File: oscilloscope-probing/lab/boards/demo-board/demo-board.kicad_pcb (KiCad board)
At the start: 8 copper layers, 126 x 117 mm, 298 parts, among them J1 CONN_01X03, J10 SMA-J-P-H-ST-EM1, J11 TESTCLIP, J12 TESTCLIP, J13 TESTCLIP, J14 USB_C_Receptacle_USB2.0, J15 TESTCLIP, J16 SMA-J-P-H-ST-EM1, J17 SMA-J-P-H-ST-EM1, J18 SMA-J-P-H-ST-EM1, J19 SMA-J-P-H-ST-EM1, J2 CORTEX_DEBUG_ETM, J20 SMA-J-P-H-ST-EM1, J21 SMA-J-P-H-ST-EM1, J3 XILINX_JTAG, J4 CORTEX_DEBUG_ETM, J5 DISPLAY, J6 CONN_01X06, J7 SMA-J-P-H-ST-EM1, J8 SMA-J-P-H-ST-EM1, J9 SMA-J-P-H-ST-EM1, M1 LOGO, M2 LOGO, M3 LOGO, M4 LOGO, Q1 SSM6N58NU, SW1 SWITCH, SW2 SWITCH, SW3 SWITCH, SW4 SWITCH, SW5 SWITCH, SW6 SWITCH, SW7 SWITCH, U1 FT234XD, U10 19-C47/RSGHBHC-5V01/2T, U11 19-C47/RSGHBHC-5V01/2T, U12 19-C47/RSGHBHC-5V01/2T, U13 19-C47/RSGHBHC-5V01/2T, U2 STM32L431-QFN48, U26 74LVC1T45, U3 LTC3374A, U39 NCP45525IMNTWG-H, U4 XC7A35T-2FGG484I, U5 STM32H750XBH6, U6 ECS-1612MV-250-CN, U7 ECS-1612MV-250-CN, U8 S25FL064LABMFI013, U9 SIT9121AI-2BF-XXS156.250000G

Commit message: Continued demo board layout
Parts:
- added C124: 0.1 uF, azonenberg_pcb:EIA_0402_CAP_NOSILK, F.Cu at (33.0, 92.5)
- added C125: 0.1 uF, azonenberg_pcb:EIA_0402_CAP_NOSILK, F.Cu at (33.0, 76.5)
- added J22: SMA-J-P-H-ST-EM1, azonenberg_pcb:CONN_SMA_EDGE_SAMTEC_SMA_J_P_H_ST_EM1, F.Cu at (60.5, 29.5)
- added J23: SMA-J-P-H-ST-EM1, azonenberg_pcb:CONN_SMA_EDGE_SAMTEC_SMA_J_P_H_ST_EM1, F.Cu at (60.5, 35.5)
- C16, C17, C53, R37, R5: moved to B.Cu
- moved TP2 144.0 mm to (57.2, 81.5), turned to 90 degrees
- moved R37 134.5 mm to (59.0, 59.5), turned to -90 degrees
- moved J6 123.3 mm to (76.5, 37.0), turned to 180 degrees
- moved C16 114.0 mm to (59.2, 65.5)
- moved C17 114.0 mm to (59.2, 67.5)
- moved C53 113.6 mm to (61.5, 60.5)
- moved R35 99.2 mm to (76.2, 70.8), turned to 180 degrees
- moved TP8 77.4 mm to (97.5, 87.5), turned to 180 degrees
- moved D4 13.2 mm to (110.2, 63.8)
- moved D5 13.2 mm to (110.2, 64.8)
- moved D6 13.2 mm to (110.2, 65.8)
- moved D7 13.2 mm to (110.2, 66.8)
- moved R39 13.2 mm to (108.2, 63.8)
- moved R41 13.2 mm to (108.2, 64.8)
- moved R42 13.2 mm to (108.2, 65.8)
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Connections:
- J20 pad 1: /Test signals/2XTHRU -> /Test signals/GTP_TX1_AC_P
- J21 pad 1: /Test signals/2XTHRU -> /Test signals/GTP_TX1_AC_N
- U2 pad 29: unconnected-(U2A-PA8-Pad29) -> /MCU/MCU_RST_N
- U2 pad 32: unconnected-(U2A-PA11-Pad32) -> /FPGA support/FPGA_RST_N
- U2 pad 41: /MCU/MCU_RST_N -> /FPGA support/FPGA_INIT
- U2 pad 42: /FPGA support/FPGA_RST_N -> /Power Supply/SUPER_I2C_SCL
- U2 pad 43: /FPGA support/FPGA_INIT -> /Power Supply/SUPER_I2C_SDA
- U4 pad AA18: /MCU/FMC_NE3 -> /MCU/FMC_A17
- U4 pad AA20: /MCU/FMC_NOE -> /MCU/FMC_A16
- U4 pad AA21: /MCU/FMC_NWE -> /MCU/FMC_AD1
- U4 pad AB18: /MCU/FMC_AD0 -> /MCU/FMC_A18
- U4 pad AB20: /MCU/FMC_NE4 -> /MCU/FMC_AD14
- U4 pad AB21: /MCU/FMC_A16 -> /MCU/FMC_AD13
- U4 pad AB22: /MCU/FMC_A17 -> /MCU/FMC_AD15
- U4 pad C5: unconnected-(U4I-GTP_TX_1_N-PadC5) -> /Test signals/GTP_TX1_N
- U4 pad D5: unconnected-(U4I-GTP_TX_1_P-PadD5) -> /Test signals/GTP_TX1_P
- U4 pad N13: /MCU/FMC_AD11 -> /MCU/FMC_NBL0
- U4 pad N14: /MCU/FMC_AD12 -> /MCU/FMC_NBL1
- U4 pad N15: /MCU/FMC_AD15 -> /MCU/FMC_NE3
- U4 pad P15: /MCU/FMC_AD9 -> /MCU/FMC_A22
- U4 pad P16: /MCU/FMC_AD13 -> /MCU/FMC_NOE
- U4 pad P17: /MCU/FMC_AD8 -> /MCU/FMC_AD6
- U4 pad R14: /MCU/FMC_AD4 -> /MCU/FMC_NL_NADV
- U4 pad R16: /MCU/FMC_AD10 -> /MCU/FMC_NWAIT
- U4 pad R17: /MCU/FMC_AD14 -> /MCU/FMC_NE4
- U4 pad R18: /MCU/FMC_AD5 -> /MCU/FMC_A20
- U4 pad T18: /MCU/FMC_AD6 -> /MCU/FMC_AD8
- U4 pad U17: /MCU/FMC_AD1 -> /MCU/FMC_NWE
- U4 pad U20: /MCU/FMC_A18 -> /MCU/FMC_NE2
- U4 pad U21: /MCU/FMC_A22 -> /MCU/FMC_AD9
- U4 pad V22: /MCU/FMC_A20 -> /MCU/FMC_AD5
- U4 pad W17: /MCU/FMC_NE2 -> /MCU/FMC_AD0
- U4 pad W21: /MCU/FMC_NL_NADV -> /MCU/FMC_AD4
- U4 pad W22: /MCU/FMC_NWAIT -> /MCU/FMC_AD10
- U4 pad Y21: /MCU/FMC_NBL0 -> /MCU/FMC_AD11
- U4 pad Y22: /MCU/FMC_NBL1 -> /MCU/FMC_AD12
- U5 pad A2: unconnected-(U5I-PI6-PadA2) -> /MCU/MCU_LED0
- U5 pad A3: unconnected-(U5I-PI5-PadA3) -> /MCU/MCU_LED1
- U5 pad A4: unconnected-(U5I-PI4-PadA4) -> /MCU/MCU_LED2
- U5 pad A5: unconnected-(U5B-PB5-PadA5) -> /MCU/MCU_LED3
- U5 pad N6: /MCU/MCU_LED0 -> unconnected-(U5J-PJ0-PadN6)
- U5 pad P6: /MCU/MCU_LED1 -> unconnected-(U5J-PJ1-PadP6)
- U5 pad T6: /MCU/MCU_LED2 -> unconnected-(U5J-PJ2-PadT6)
- U5 pad U6: /MCU/MCU_LED3 -> unconnected-(U5J-PJ3-PadU6)
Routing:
- net /GND: track 827.9 -> 874.3 mm, vias 373 -> 378
- net /MCU/DPAD_N: track 20.5 -> 59.5 mm
- net /MCU/DPAD_W: track 33.2 -> 71.4 mm
- net /MCU/DPAD_SEL: track 27.0 -> 64.9 mm
- net /MCU/DPAD_S: track 35.7 -> 72.6 mm
- net /MCU/DPAD_E: track 24.8 -> 60.7 mm
- net /Power Supply/1V0_FB: track 2.79 -> 36.8 mm, vias 2 -> 3
- net /USB power inlet and UART/UART_TX: track 12.9 -> 45.6 mm
- net /MCU/FMC_AD7: track 0.00 -> 32.0 mm
- net /USB power inlet and UART/UART_RX: track 17.5 -> 47.7 mm
- net /MCU/FMC_AD6: track 0.00 -> 30.1 mm
- net /MCU/FMC_AD0: track 5.03 -> 34.0 mm
- net /USB power inlet and UART/UART_RTS_N: track 21.9 -> 49.6 mm
- net /USB power inlet and UART/UART_CTS_N: track 22.8 -> 49.3 mm
- net /MCU/FMC_A18: track 2.00 -> 28.2 mm
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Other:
- board text added: "1V0"
- board text added: "MCU LED"
- board text added: "MCU UART"
- board text added: "SCL"
- board text added: "SDA"
- board text added: "SUPER STATUS"

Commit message: Continued routing demo board
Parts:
- C90, C92, C95, R38, U9: moved to B.Cu
- moved U9 148.7 mm to (42.9, 62.0)
- moved C90 148.2 mm to (40.0, 62.0), turned to 90 degrees
- moved C95 142.9 mm to (46.2, 61.0)
- moved C92 142.3 mm to (46.2, 62.5)
- moved R22 130.1 mm to (69.2, 88.6)
- moved R23 129.8 mm to (69.2, 89.6), turned to 180 degrees
- moved R24 127.5 mm to (69.2, 86.2)
- moved R25 127.3 mm to (69.2, 87.2), turned to 180 degrees
- moved J3 114.2 mm to (54.5, 43.5), turned to 180 degrees
- moved TP9 79.1 mm to (110.8, 78.2), turned to -90 degrees
- moved R38 71.1 mm to (104.4, 69.0), turned to 90 degrees
- moved U26 50.4 mm to (222.8, 70.0)
- moved C65 33.2 mm to (90.2, 66.2), turned to 180 degrees
- moved C64 27.9 mm to (101.8, 79.2), turned to -90 degrees
- moved J4 27.0 mm to (136.2, 68.5), turned to 90 degrees
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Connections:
- U4 pad F21: unconnected-(U4F-IO_25_16-PadF21) -> /Test signals/LED_CTRL
- U5 pad D10: /MCU/DPAD_SEL -> unconnected-(U5J-PJ14-PadD10)
- U5 pad D11: /MCU/DPAD_S -> unconnected-(U5J-PJ12-PadD11)
- U5 pad E10: /MCU/DPAD_N -> unconnected-(U5J-PJ13-PadE10)
- U5 pad L14: /MCU/DPAD_W -> /MCU/DPAD_S
- U5 pad M14: unconnected-(U5J-PJ9-PadM14) -> /MCU/DPAD_SEL
- U5 pad N14: unconnected-(U5J-PJ7-PadN14) -> /MCU/DPAD_W
- U5 pad N15: unconnected-(U5J-PJ6-PadN15) -> /MCU/DPAD_N
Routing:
- net /MCU/TRACED3: track 0.00 -> 42.2 mm, vias 0 -> 2
- net /GND: track 874.3 -> 915.8 mm, vias 378 -> 394
- net /MCU/TRACED2: track 0.00 -> 41.2 mm, vias 0 -> 2
- net /MCU/TRACED0: track 0.00 -> 35.5 mm, vias 1 -> 2
- net /MCU/TRACED1: track 0.00 -> 35.3 mm, vias 1 -> 2
- net /MCU/JTAG_TDO: track 0.00 -> 34.2 mm, vias 0 -> 2
- net /Power Supply/SUPER_I2C_SDA: track 5.68 -> 37.2 mm, vias 1 -> 2
- net /Power Supply/SUPER_I2C_SCL: track 7.99 -> 38.4 mm, vias 1 -> 2
- net /MCU/DPAD_E: track 60.7 -> 86.7 mm
- net /MCU/DPAD_S: track 72.6 -> 97.4 mm
- net /MCU/DPAD_SEL: track 64.9 -> 88.5 mm
- net /MCU/DPAD_W: track 71.4 -> 94.2 mm
- net /MCU/TRACECLK: track 8.48 -> 31.0 mm, vias 1 -> 2
- net /MCU/DPAD_N: track 59.5 -> 80.4 mm
- net /3V3: track 561.4 -> 578.8 mm, vias 90 -> 93
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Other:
- board text added: "MCU DEBUG"
- board text added: "VCORE"

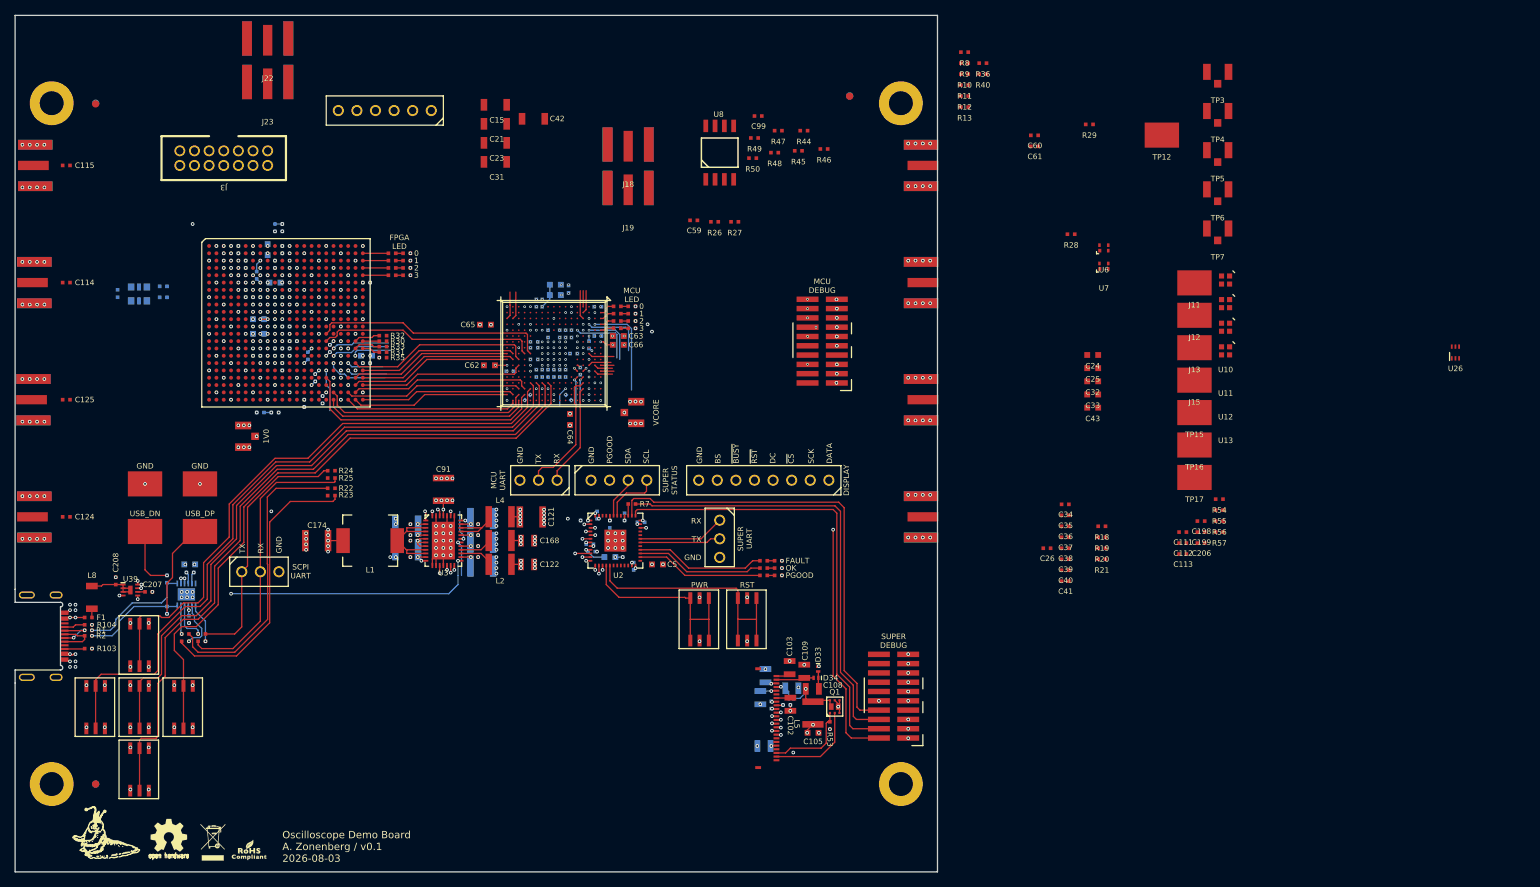
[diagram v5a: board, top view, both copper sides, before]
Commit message: Continued demo board layout
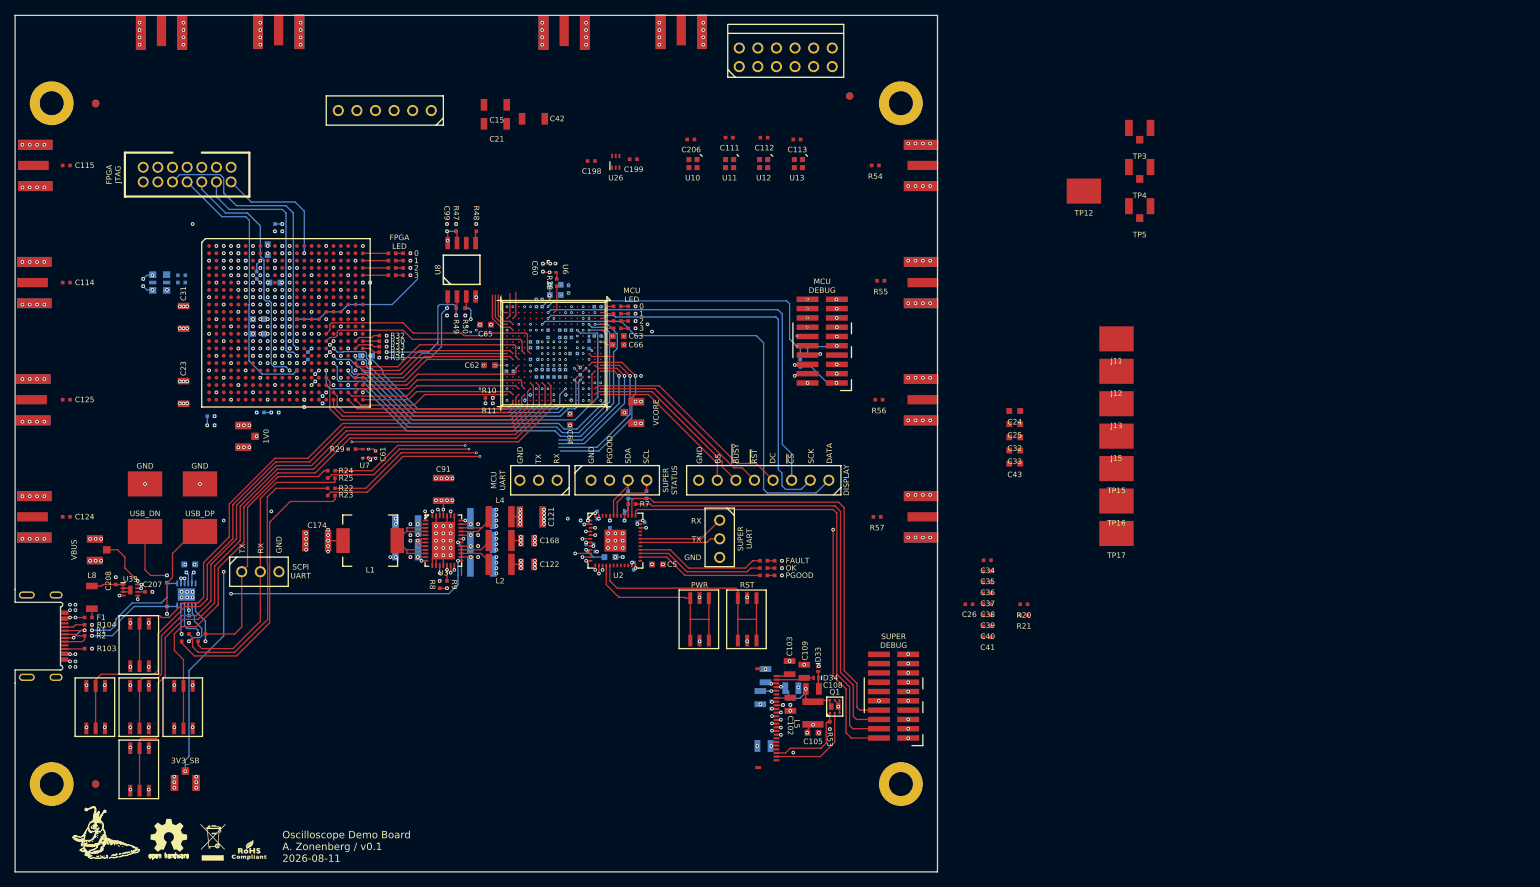
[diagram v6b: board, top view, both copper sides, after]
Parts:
- added J24: PMOD_HOST, azonenberg_pcb:CONN_HEADER_2.54MM_2x6_RA_PMOD_HOST, F.Cu at (131.3, 29.7)
- C59, R12, R13, R18, R19, R26, R27, R36, R40, R44, R45, R46: moved to B.Cu
- J18, J19, J22, J23: footprint azonenberg_pcb:CONN_SMA_EDGE_SAMTEC_SMA_J_P_H_ST_EM1 -> azonenberg_pcb:CONN_SMA_EDGE_SAMTEC_SMA_J_P_H_ST_EM1_NOPASTE
- moved TP6 161.0 mm to (37.0, 97.0), turned to 90 degrees
- moved TP7 160.0 mm to (49.2, 128.8), turned to 180 degrees
- moved U26 117.6 mm to (108.0, 44.0)
- moved R19 114.4 mm to (64.0, 65.5), turned to 180 degrees
- moved R18 112.1 mm to (64.5, 72.0), turned to 90 degrees
- moved R12 111.8 mm to (52.8, 78.8), turned to 180 degrees
- moved R13 111.7 mm to (52.8, 80.0)
- moved R29 110.1 mm to (72.0, 83.2)
- moved U7 104.0 mm to (73.9, 83.8), turned to 90 degrees
- moved R8 102.1 mm to (84.0, 101.8), turned to 90 degrees
- moved R9 100.4 mm to (85.0, 101.8), turned to -90 degrees
- moved C61 99.4 mm to (75.2, 84.0), turned to 90 degrees
- moved C198 96.7 mm to (104.7, 43.9)
- moved C199 92.8 mm to (110.5, 43.6)
- moved C206 88.9 mm to (118.3, 41.0)
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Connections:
- C92 pad 2: /Test signals/GTP_REF_P -> /Test signals/GTP_REF_N
- C95 pad 2: /Test signals/GTP_REF_N -> /Test signals/GTP_REF_P
- J6 pad 2: /MCU/FPGA_UART_CTS_N -> /Test signals/FPGA_UART_CTS_N
- J6 pad 4: /MCU/FPGA_UART_TX -> /Test signals/FPGA_UART_TX
- J6 pad 5: /MCU/FPGA_UART_RX -> /Test signals/FPGA_UART_RX
- J6 pad 6: /MCU/FPGA_UART_RTS_N -> /Test signals/FPGA_UART_RTS_N
- U4 pad A18: unconnected-(U4F-IO_L17P_T2_16-PadA18) -> /Test signals/FPGA_UART_CTS_N
- U4 pad A19: unconnected-(U4F-IO_L17N_T2_16-PadA19) -> /Test signals/FPGA_UART_TX
- U4 pad A20: unconnected-(U4F-IO_L16N_T2_16-PadA20) -> /Test signals/FPGA_UART_RTS_N
- U4 pad A21: unconnected-(U4F-IO_L21N_T3_DQS_16-PadA21) -> /Test signals/FPGA_UART_RX
- U4 pad AA19: /MCU/FPGA_UART_RTS_N -> unconnected-(U4D-IO_L15P_T2_DQS_RDWR_B_14-PadAA19)
- U4 pad N13: /MCU/FMC_NBL0 -> /MCU/FMC_A21
- U4 pad N14: /MCU/FMC_NBL1 -> /MCU/FMC_A20
- U4 pad N15: /MCU/FMC_NE3 -> /MCU/FMC_A19
- U4 pad P15: /MCU/FMC_A22 -> /MCU/FMC_AD8
- U4 pad P19: /MCU/FPGA_UART_TX -> unconnected-(U4D-IO_L5P_T0_D06_14-PadP19)
- U4 pad R14: /MCU/FMC_NL_NADV -> /MCU/FMC_NE1
- U4 pad R18: /MCU/FMC_A20 -> /MCU/FMC_NE3
- U4 pad R19: /MCU/FPGA_UART_RX -> unconnected-(U4D-IO_L5N_T0_D07_14-PadR19)
- U4 pad T18: /MCU/FMC_AD8 -> /MCU/FMC_AD2
- U4 pad T21: /MCU/FMC_A21 -> /MCU/FMC_NE2
- U4 pad U18: /MCU/FMC_AD2 -> /MCU/FMC_NBL0
- U4 pad U20: /MCU/FMC_NE2 -> /MCU/FMC_A22
- U4 pad V17: /MCU/FMC_NE1 -> /MCU/FMC_NBL1
- U4 pad V19: /MCU/FPGA_UART_CTS_N -> unconnected-(U4D-IO_L14N_T2_SRCC_14-PadV19)
- U4 pad V20: /MCU/FMC_A19 -> /MCU/FMC_NL_NADV
- U5 pad A15: unconnected-(U5I-PI1-PadA15) -> /MCU/DPY_RST_N
- U5 pad A16: /MCU/MCU_TRIG -> /MCU/DPY_BS
- U5 pad B15: unconnected-(U5I-PI2-PadB15) -> /MCU/DPY_DC
- U5 pad B16: unconnected-(U5H-PH15-PadB16) -> /MCU/DPY_BUSY_N
- U5 pad E4: unconnected-(U5I-PI8-PadE4) -> /MCU/MCU_TRIG
- U5 pad H4: /MCU/DPY_BS -> unconnected-(U5F-PF3-PadH4)
- U5 pad J4: /MCU/DPY_DC -> unconnected-(U5F-PF5-PadJ4)
- U5 pad J5: /MCU/DPY_BUSY_N -> unconnected-(U5F-PF4-PadJ5)
- U5 pad K4: /MCU/DPY_RST_N -> unconnected-(U5F-PF8-PadK4)
- U5 pad N2: unconnected-(U5H-PH2-PadN2) -> /MCU/MCU_PMOD_DQ5
- U5 pad P2: unconnected-(U5H-PH3-PadP2) -> /MCU/MCU_PMOD_DQ6
- U5 pad P3: unconnected-(U5H-PH4-PadP3) -> /MCU/MCU_PMOD_DQ7
- U5 pad R3: unconnected-(U5A-PA6-PadR3) -> /MCU/MCU_PMOD_DQ4
- U5 pad T4: unconnected-(U5C-PC4-PadT4) -> /MCU/MCU_PMOD_DQ3
- U5 pad T5: unconnected-(U5B-PB1-PadT5) -> /MCU/MCU_PMOD_DQ1
- U5 pad U2: unconnected-(U5A-PA3-PadU2) -> /MCU/MCU_PMOD_DQ2
- U5 pad U4: unconnected-(U5C-PC5-PadU4) -> /MCU/MCU_PMOD_DQ0
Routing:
- net /GND: track 915.8 -> 1273.0 mm, vias 394 -> 454
- net /3V3: track 578.8 -> 730.9 mm, vias 93 -> 107
- net /MCU/DPY_SPI_DATA: track 35.6 -> 97.0 mm, vias 1 -> 2
- net /MCU/DPY_SPI_SCK: track 35.5 -> 94.9 mm, vias 1 -> 2
- net /MCU/DPY_SPI_CS_N: track 37.0 -> 92.6 mm, vias 1 -> 2
- net /Power Supply/1V8_FB: track 5.10 -> 55.9 mm, vias 1 -> 3
- net /MCU/FMC_NBL0: track 8.53 -> 57.2 mm, vias 1 -> 2
- net /MCU/FMC_NBL1: track 13.6 -> 59.3 mm, vias 1 -> 2
- net /MCU/FMC_CLK: track 2.57 -> 48.2 mm, vias 1 -> 2
- net /MCU/FMC_NL_NADV: track 7.85 -> 51.9 mm, vias 1 -> 2
- net /MCU/MCU_RST_N: track 0.00 -> 43.4 mm, vias 0 -> 2
- net /MCU/FMC_A22: track 8.85 -> 50.7 mm, vias 1 -> 2
- net /MCU/UART_TX: track 5.17 -> 45.4 mm, vias 1 -> 3
- net /MCU/UART_RX: track 4.57 -> 44.6 mm, vias 1 -> 3
- net /MCU/UART_CTS_N: track 2.40 -> 42.3 mm, vias 1 -> 3
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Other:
- board text added: "3V3_SB"
- board text added: "FPGA JTAG"
- board text added: "Oscilloscope Demo Board A. Zonenberg / v0.1 2026-08-11"
- board text added: "VBUS"
- board text removed: "Oscilloscope Demo Board A. Zonenberg / v0.1 2026-08-03"
